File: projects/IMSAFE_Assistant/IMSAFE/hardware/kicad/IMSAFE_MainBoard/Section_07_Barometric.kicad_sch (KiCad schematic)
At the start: 0 parts

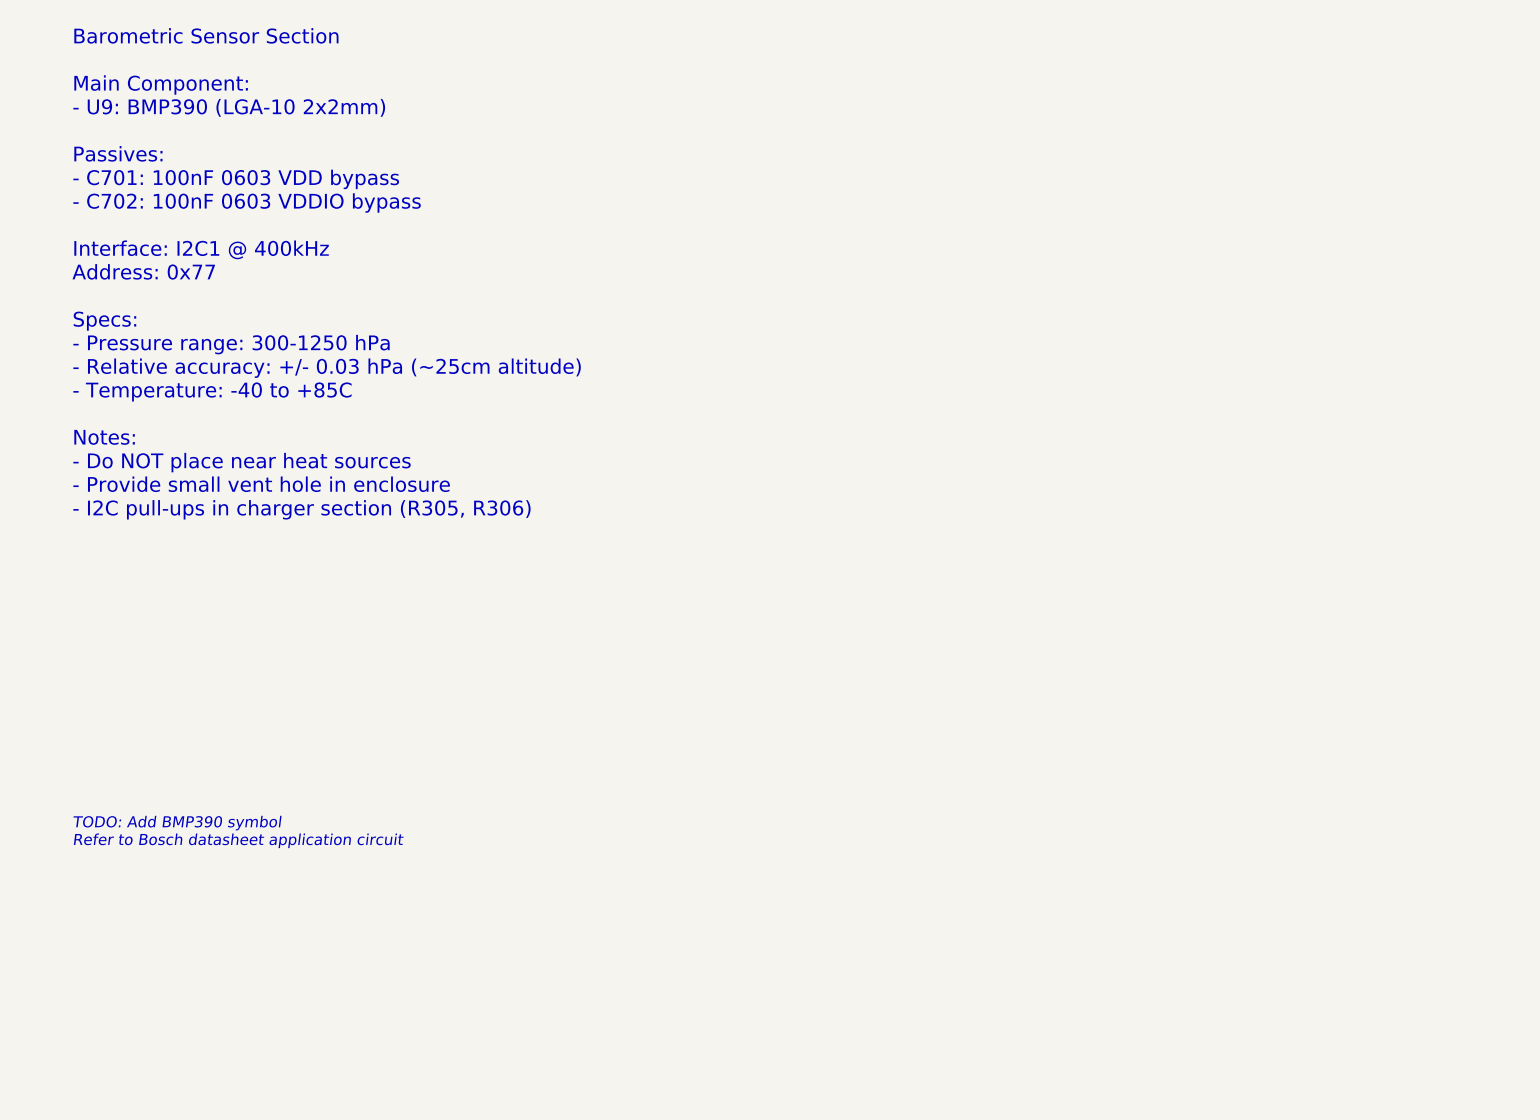
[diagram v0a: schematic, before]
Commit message: Add Sections 07, 14-16: Barometric, I/O expander, LEDs, encoders
Complete schematic sections for:
- Section 07: BMP390 barometric pressure sensor (I2C)
- Section 14: MCP23017 I/O expander with 8 toggle switches
- Section 15: WS2812B-2020 addressable RGB status LEDs (x16)
- Section 16: EC11 rotary encoders with hardware debouncing

All sections include JLCPCB part numbers and hierarchical labels
for integration with main schematic.

Co-Authored-By: Claude Opus 4.5 <noreply@anthropic.com>
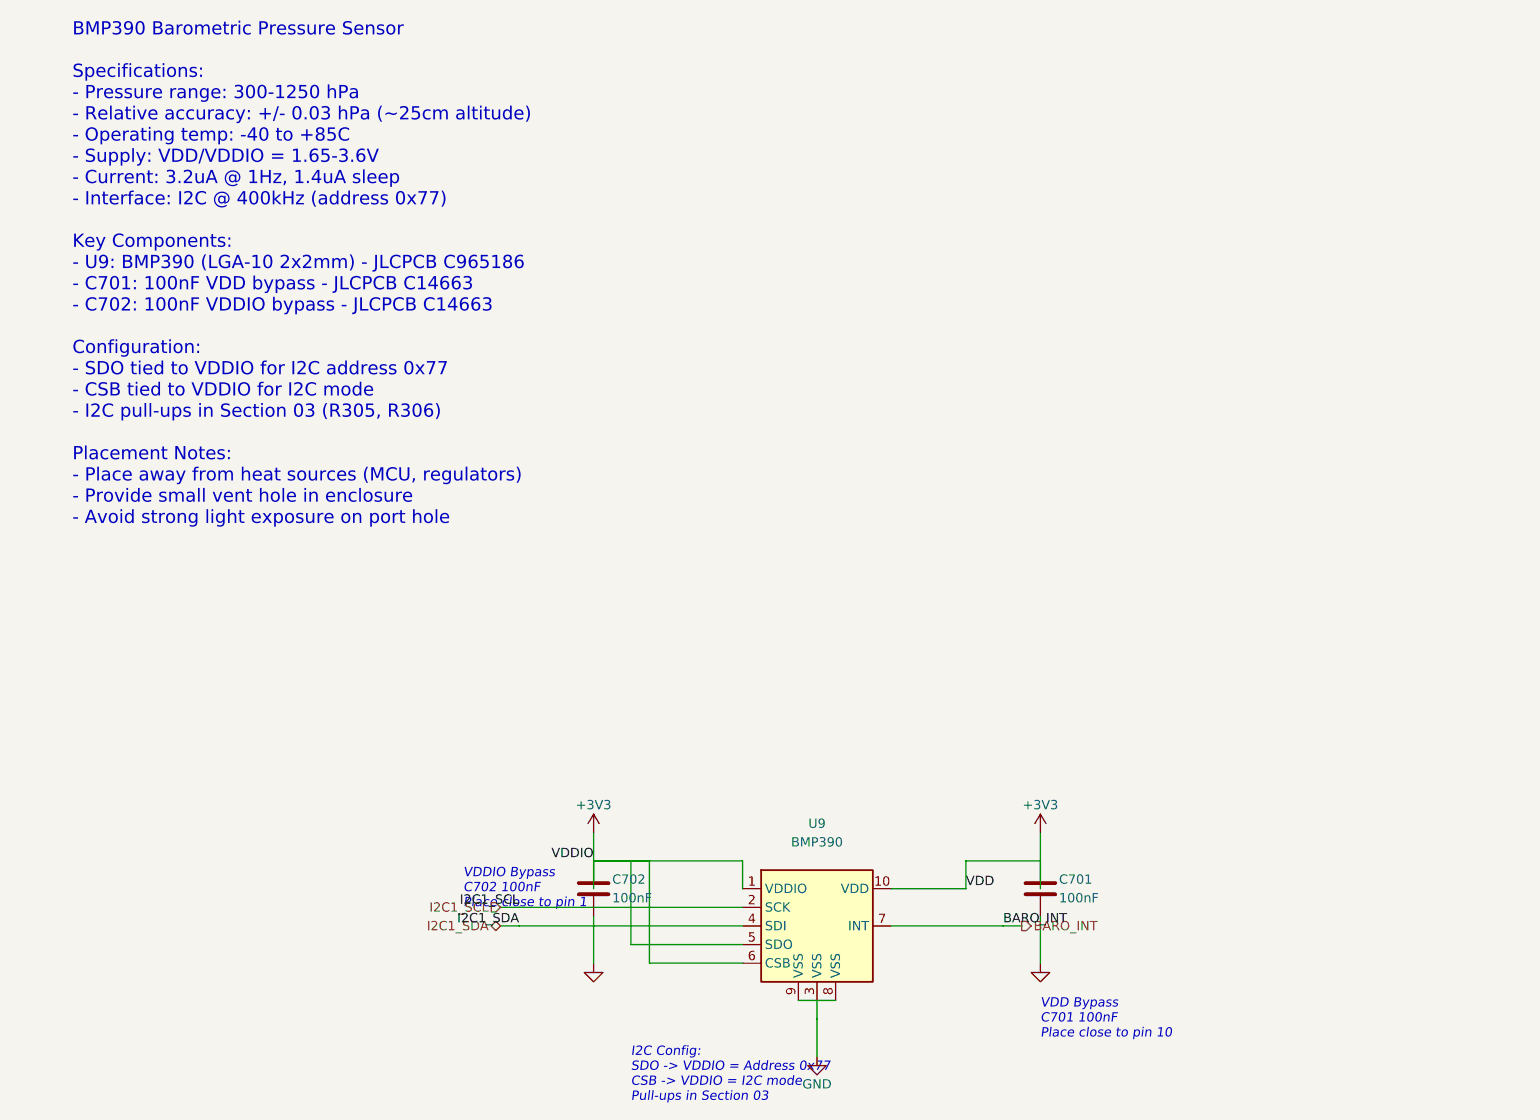
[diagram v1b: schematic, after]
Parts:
- added C701, C702: 100nF, Capacitor_SMD:C_0603_1608Metric, symbol Device:C
- added U9: BMP390, Package_LGA:Bosch_LGA-10_2x2.5mm_P0.5mm, symbol Sensor:BMP390
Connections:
- new net +3V3: C701.1, C702.1, U9.1 (VDDIO), U9.10 (VDD), U9.5 (SDO), U9.6 (CSB)
- new net BARO_INT: U9.7 (INT)
- new net GND: C701.2, C702.2, U9.3 (VSS), U9.8 (VSS), U9.9 (VSS)
- new net I2C1_SCL: U9.2 (SCK)
- new net I2C1_SDA: U9.4 (SDI)
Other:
- note added: "BMP390 Barometric Pressure Sensor Specifications: - Pressure range: 300-1250 hPa - Relative accuracy: +/- 0.03 hPa (~25cm altitude) - Operating temp: -40 to +85C - Supply: VDD/VDDIO = 1.65-3.6V - Current: 3.2uA @ 1Hz, 1.4uA sleep - Interface: I2C @ 400kHz (address 0x77) Key Components: - U9: BMP390 (LGA-10 2x2mm) - JLCPCB C965186 - C701: 100nF VDD bypass - JLCPCB C14663 - C702: 100nF VDDIO bypass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"
- note added: "I2C Config: SDO -> VDDIO = Address 0x77 CSB -> VDDIO = I2C mode Pull-ups in Section 03"
- note added: "VDD Bypass C701 100nF Place close to pin 10"
- note added: "VDDIO Bypass C702 100nF Place close to pin 1"
- note removed: "Barometric Sensor Section Main Component: - U9: BMP390 (LGA-10 2x2mm) Passives: - C701: 100nF 0603 VDD bypass - C702: 100nF 0603 VDDIO bypass Interface: I2C1 @ 400kHz Address: 0x77 Specs: - Pressure range: 300-1250 hPa - Relative accuracy: +/- 0.03 hPa (~25cm altitude) - Temperature: -40 to +85C Notes: - Do NOT place near heat sources - Provide small vent hole in enclosure - I2C pull-ups in charg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"
- note removed: "TODO: Add BMP390 symbol Refer to Bosch datasheet application circuit"

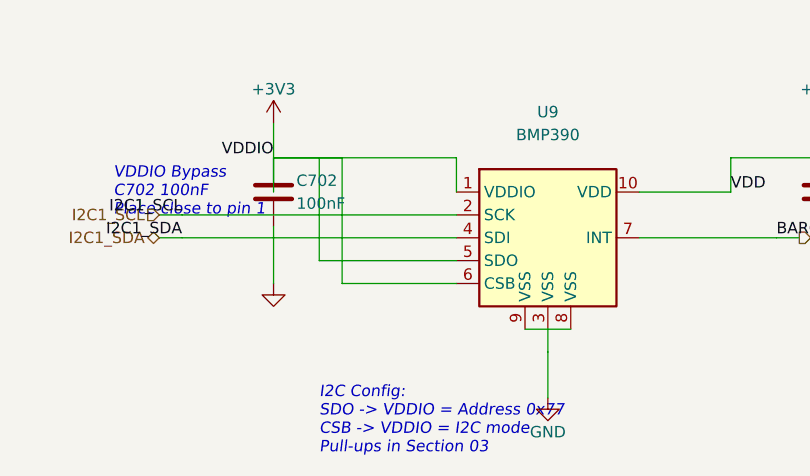
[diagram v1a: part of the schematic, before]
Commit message: Fix ERC errors across multiple schematic sections
- Section_04_BMS: Add VSYS hierarchical label for root schematic connection
- Section_05/06 Regulators: Add PWR_FLAG wire and junction to VSYS net
- Section_07_Barometric: Connect BMP390 SCK pin to GND for I2C mode
- Section_14_IO_Expander: Add no-connect symbols for unused MCP23017 GPIO pins
- Update design-rationale.md with ERC remediation status

Co-Authored-By: Claude Opus 4.5 <noreply@anthropic.com>
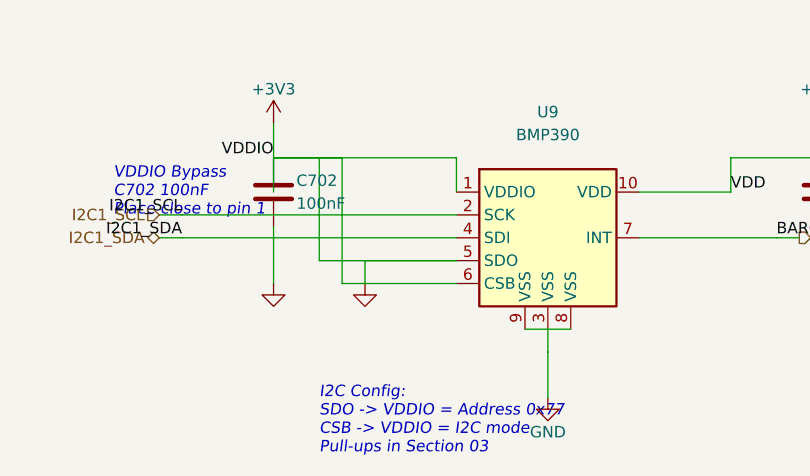
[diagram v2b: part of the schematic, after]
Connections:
- net GND is gone; now on net +3V3: C701.2, C702.2, U9.3 (VSS), U9.8 (VSS), U9.9 (VSS)
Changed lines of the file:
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@@
 		(instances (project "IMSAFE_MainBoard" (path "/sec07-0001-0002-0003-000000000001" (reference "#PWR0705") (unit 1))))
+	)
+	(symbol (lib_id "power:GND") (at 106.68 119.38 0) (unit 1)
+		(exclude_from_sim no) (in_bom yes) (on_board yes) (dnp no)
+		(uuid "pwr-gnd-sck")
+		(property "Reference" "#PWR0706" (at 106.68 125.73 0) (effects (font (size 1.27 1.27)) hide))
+		(property "Value" "GND" (at 106.68 123.19 0) (effects (font (size 1.27 1.27)) hide))
+		(property "Footprint" "" (at 106.68 119.38 0) (effects (font (size 1.27 1.27)) hide))
+		(property "Datasheet" "" (at 106.68 119.38 0) (effects (font (size 1.27 1.27)) hide))
+		(pin "1" (uuid "pwr-gnd-sck-p1"))
+		(instances (project "IMSAFE_MainBoard" (path "/sec07-0001-0002-0003-000000000001" (reference "#PWR0706") (unit 1))))
 	)
 	(wire (pts (xy 96.52 101.6) (xy 96.52 105.41)) (stroke (width 0) (type default)) (uuid "w-3v3-c702-top"))
@@
 	(wire (pts (xy 104.14 119.38) (xy 104.14 105.41)) (stroke (width 0) (type default)) (uuid "w-csb-vert"))
 	(wire (pts (xy 104.14 105.41) (xy 101.6 105.41)) (stroke (width 0) (type default)) (uuid "w-csb-vddio"))
+	(wire (pts (xy 116.84 116.84) (xy 106.68 116.84)) (stroke (width 0) (type default)) (uuid "w-sck-horiz"))
+	(wire (pts (xy 106.68 116.84) (xy 106.68 119.38)) (stroke (width 0) (type default)) (uuid "w-sck-gnd"))
 	(wire (pts (xy 116.84 111.76) (xy 86.36 111.76)) (stroke (width 0) (type default)) (uuid "w-scl-u9"))
 	(wire (pts (xy 116.84 114.3) (xy 86.36 114.3)) (stroke (width 0) (type default)) (uuid "w-sda-u9"))

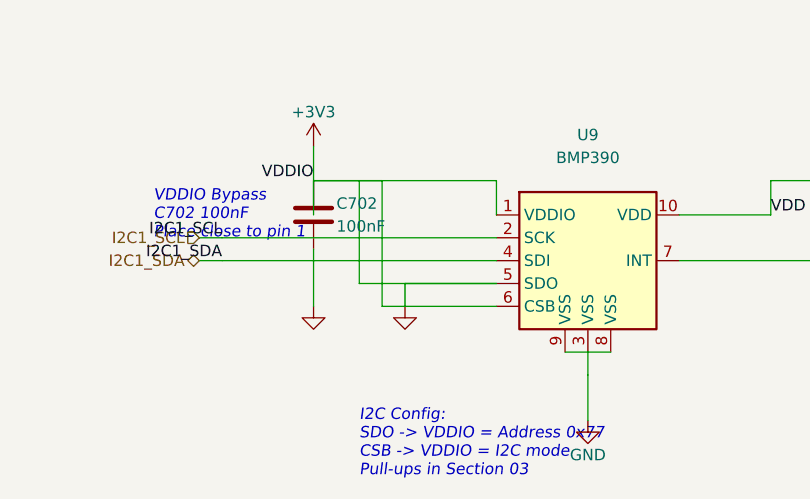
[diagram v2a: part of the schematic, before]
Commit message: Add sensor and interface schematic implementations
- Section 01: MCU Core additional connections
- Section 04: BMS refinements
- Section 07: Barometric sensor (BMP390)
- Section 08: IMU (ICM-42688-P) full implementation
- Section 09: Magnetometer (MMC5983MA) full implementation
- Section 10: Gas sensor (MICS-4514) with heater control
- Section 11: Temp/Humidity (Si7021-A20) implementation
- Section 14: I/O Expander updates
- Section 16: Rotary encoder connections
- Section 19: Audio buzzer (MLT-8530) with MOSFET driver

Co-Authored-By: Claude Opus 4.5 <noreply@anthropic.com>
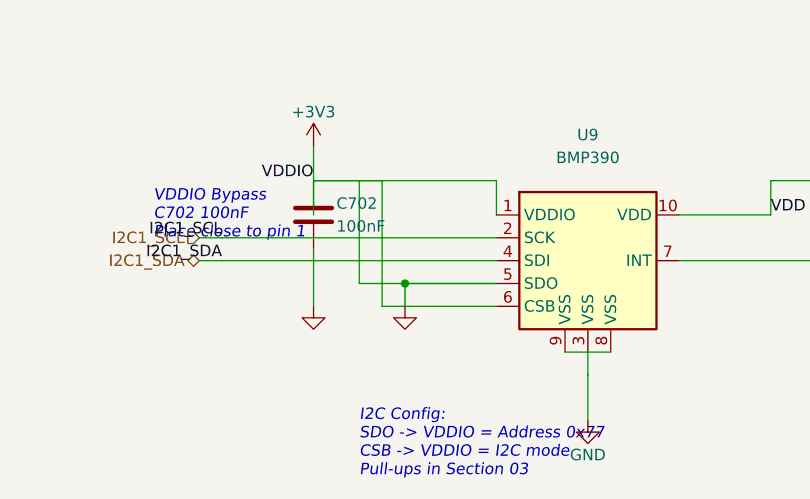
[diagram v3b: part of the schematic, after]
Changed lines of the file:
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@@
 	(wire (pts (xy 116.84 116.84) (xy 106.68 116.84)) (stroke (width 0) (type default)) (uuid "w-sck-horiz"))
 	(wire (pts (xy 106.68 116.84) (xy 106.68 119.38)) (stroke (width 0) (type default)) (uuid "w-sck-gnd"))
+	(junction (at 106.68 116.84) (diameter 0) (color 0 0 0 0) (uuid "junc-sck-gnd"))
 	(wire (pts (xy 116.84 111.76) (xy 86.36 111.76)) (stroke (width 0) (type default)) (uuid "w-scl-u9"))
 	(wire (pts (xy 116.84 114.3) (xy 86.36 114.3)) (stroke (width 0) (type default)) (uuid "w-sda-u9"))
